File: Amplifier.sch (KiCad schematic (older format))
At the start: 52 parts, among them J501 TB001-500-04BE CUI_Devices, SW501 DS04-254-2-02BK-SMT, U501 TDA7498L

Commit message: fertig zum routen
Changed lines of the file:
@@
 $EndComp
 Wire Wire Line
-	6500 3500 8250 3500
+	6500 3500 7300 3500
 Connection ~ 8250 3500
 Wire Wire Line
@@
 	1    0    0    -1
 $EndComp
+$Comp
+L power:PWR_FLAG #FLG0114
+U 1 1 5E990599
+P 7300 3500
+F 0 "#FLG0114" H 7300 3575 50  0001 C CNN
+F 1 "PWR_FLAG" H 7550 3600 50  0000 C CNN
+F 2 "" H 7300 3500 50  0001 C CNN
+F 3 "~" H 7300 3500 50  0001 C CNN
+	1    7300 3500
+	1    0    0    -1
+$EndComp
+Connection ~ 7300 3500
+Wire Wire Line
+	7300 3500 8250 3500
 $EndSCHEMATC

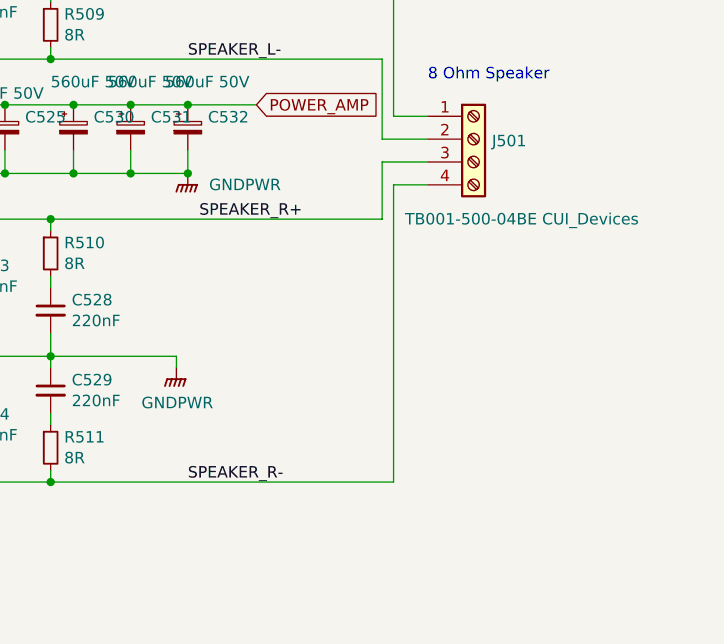
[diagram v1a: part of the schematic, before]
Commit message: Amp verdrahtet, Einige Layers verlegt
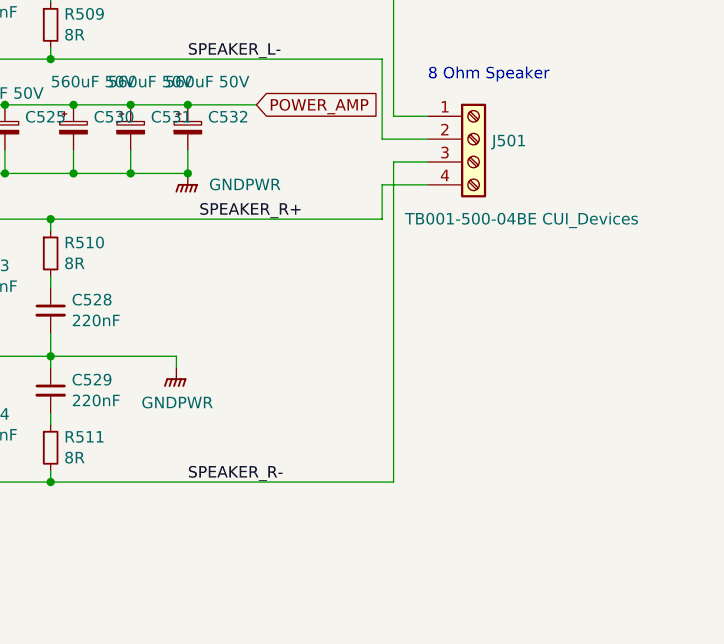
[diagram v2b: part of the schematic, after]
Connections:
- net SPEAKER_R+: now also J501.4 (Pin_4); no longer J501.3 (Pin_3)
- net SPEAKER_R-: now also J501.3 (Pin_3); no longer J501.4 (Pin_4)
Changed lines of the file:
@@
 	8450 2150 9950 2150
 Wire Wire Line
-	10100 3850 9950 3850
-Wire Wire Line
-	9950 3850 9950 5150
-Wire Wire Line
 	8450 5150 9950 5150
 Wire Wire Line
-	10100 3750 9900 3750
-Wire Wire Line
-	9900 3750 9900 4000
+	9900 3850 9900 4000
 Wire Wire Line
 	8450 4000 9900 4000
@@
 Wire Wire Line
 	7300 3500 8250 3500
+Wire Wire Line
+	9950 3750 10100 3750
+Wire Wire Line
+	9950 3750 9950 5150
+Wire Wire Line
+	9900 3850 10100 3850
 $EndSCHEMATC

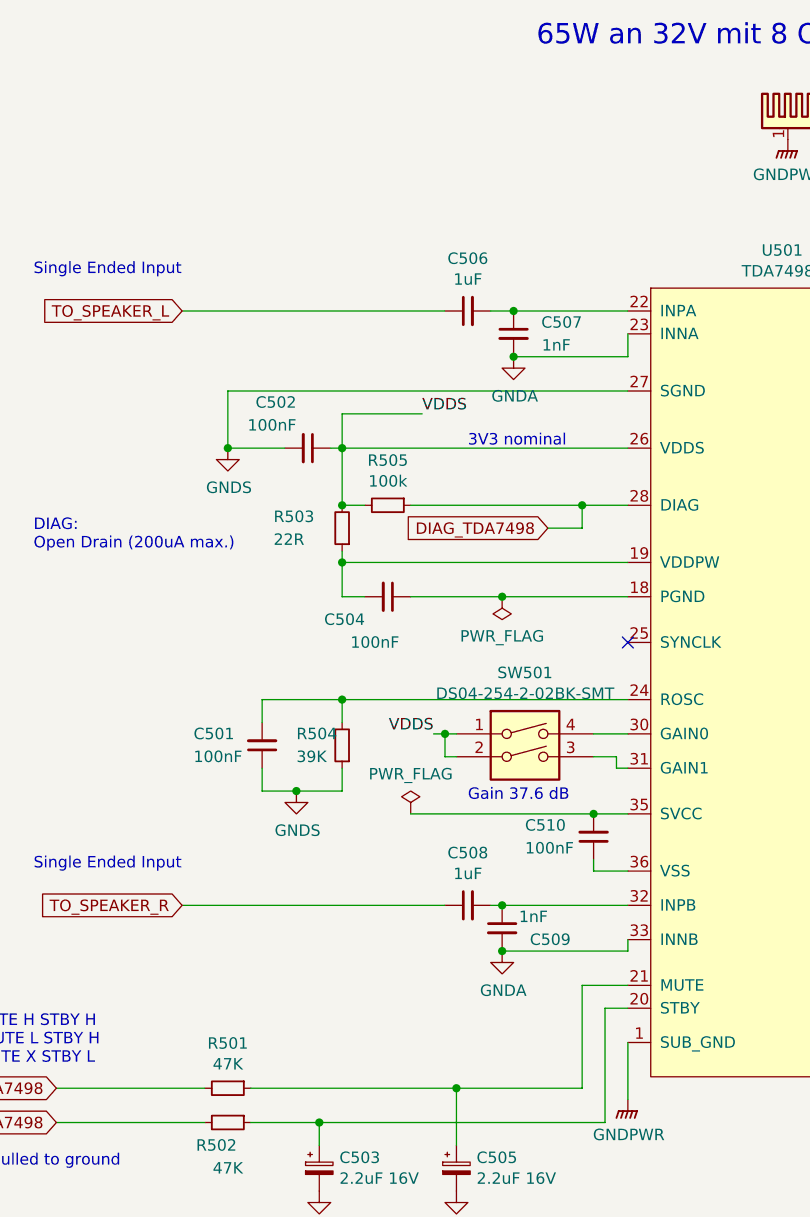
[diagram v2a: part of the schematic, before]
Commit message: Folienkondensatoren SMD gegen THT ausgetauscht. Kleine Fehler korrigiert
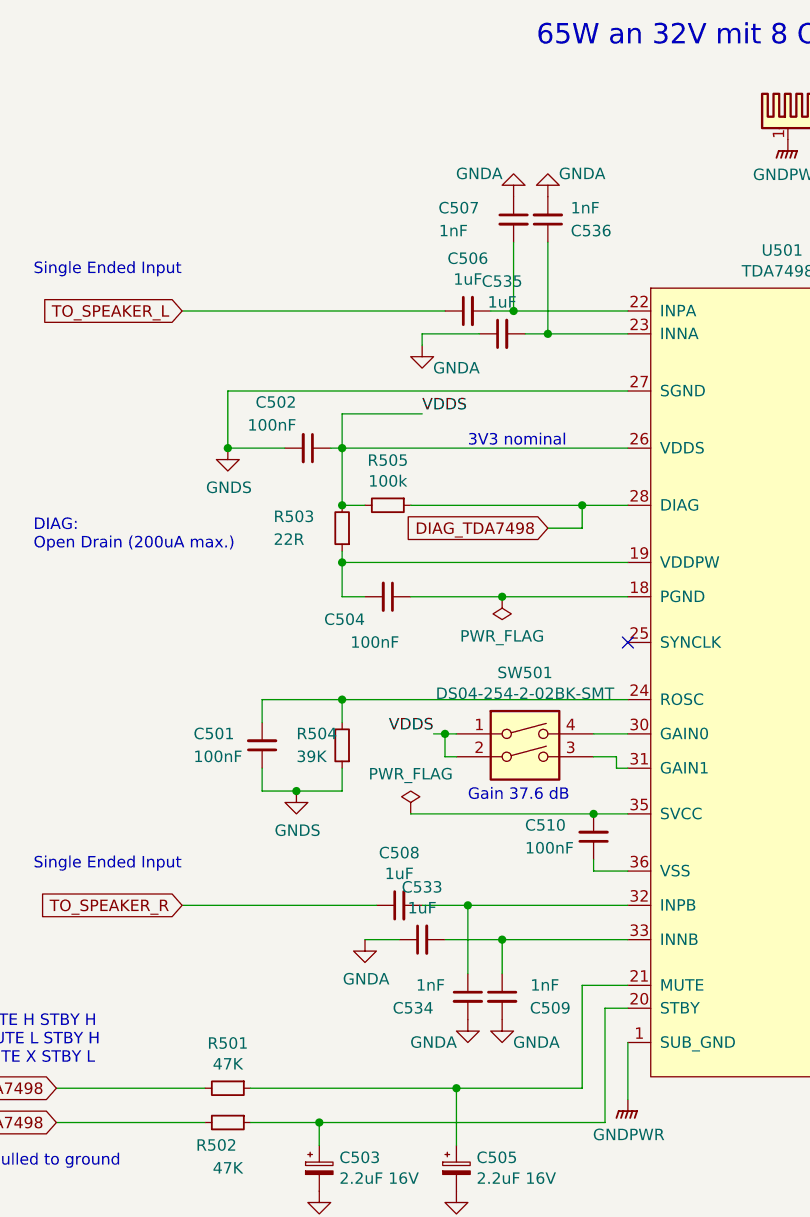
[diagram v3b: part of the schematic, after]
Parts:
- added C533, C535: 1uF, Capacitor_THT:C_Rect_L7.0mm_W2.5mm_P5.00mm, symbol Device:C_Small
- added C534, C536: 1nF, Capacitor_THT:C_Rect_L7.0mm_W2.5mm_P5.00mm, symbol Device:C_Small
- C506, C507, C508, C509, C517, C518, C519, C520, C521, C522, C523, C524, C526, C527, C528, C529: footprint Capacitor_SMD:C_0603_1608Metric_Pad1.05x0.95mm_HandSolder -> Capacitor_THT:C_Rect_L7.0mm_W2.5mm_P5.00mm
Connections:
- net GNDA: now also C507.1, C533.1, C534.2, C535.1, C536.2; no longer C507.2, U501.23 (INNA), U501.33 (INNB)
- net at C506.2, U501.22 (INPA): now also C507.2; no longer C507.1
- net at C508.2, U501.32 (INPB): now also C534.1; no longer C509.1
- new net: C535.2, C536.1, U501.23 (INNA)
- new net: C509.1, C533.2, U501.33 (INNB)
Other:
- moved on the sheet: C507, C508, C509

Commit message: layout fast fertig
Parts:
- removed C506, C508: 1uF, Capacitor_THT:C_Rect_L7.0mm_W2.5mm_P5.00mm, symbol Device:C_Small
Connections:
- net TO_SPEAKER_L: now also C507.2, U501.22 (INPA)
- net TO_SPEAKER_R: now also C534.1, U501.32 (INPB)
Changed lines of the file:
@@
 TO_SPEAKER_R
-$Comp
-L Device:C_Small C506
-U 1 1 5E7A16FA
-P 4050 2150
-F 0 "C506" V 4279 2150 50  0000 C CNN
-F 1 "1uF" V 4188 2150 50  0000 C CNN
-F 2 "Capacitor_THT:C_Rect_L7.0mm_W2.5mm_P5.00mm" H 4050 2150 50  0001 C CNN
-F 3 "~" H 4050 2150 50  0001 C CNN
-	1    4050 2150
-	0    -1   -1   0
-$EndComp
 $Comp
 L Device:C_Small C507
@@
 	4600 4600 4600 4550
 $Comp
-L Device:C_Small C508
-U 1 1 5E8A8398
-P 3750 4750
-F 0 "C508" V 3979 4750 50  0000 C CNN
-F 1 "1uF" V 3888 4750 50  0000 C CNN
-F 2 "Capacitor_THT:C_Rect_L7.0mm_W2.5mm_P5.00mm" H 3750 4750 50  0001 C CNN
-F 3 "~" H 3750 4750 50  0001 C CNN
-	1    3750 4750
-	0    -1   -1   0
-$EndComp
-$Comp
 L Device:C_Small C509
 U 1 1 5E8B9322
@@
 	1    0    0    -1
 $EndComp
-Wire Wire Line
-	3650 4750 2800 4750
 $Comp
 L Device:CP_Small C505
@@
 Wire Wire Line
 	3000 2500 4750 2500
-Wire Wire Line
-	2800 2150 3950 2150
 Text Notes 2150 4600 0    50   ~ 0
 Single Ended Input
@@
 	-1   0    0    1
 $EndComp
-Wire Wire Line
-	4150 2150 4250 2150
 $Comp
 L power:GNDA #PWR0508
@@
 	1    0    0    -1
 $EndComp
-Wire Wire Line
-	3850 4750 4050 4750
 $Comp
 L Device:C_Small C533
@@
 Wire Wire Line
 	3750 4900 3600 4900
+Wire Wire Line
+	2800 4750 4050 4750
+Wire Wire Line
+	2800 2150 4250 2150
 $EndSCHEMATC

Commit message: Fertig zum letzten Check vor Bestellung
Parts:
- C503, C505: footprint Capacitor_SMD:CP_Elec_4x5.4 -> Capacitor_THT:CP_Radial_D4.0mm_P2.00mm
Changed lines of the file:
@@
 F 0 "C505" H 4088 5946 50  0000 L CNN
 F 1 "2.2uF 16V" H 4088 5855 50  0000 L CNN
-F 2 "Capacitor_SMD:CP_Elec_4x5.4" H 4000 5900 50  0001 C CNN
+F 2 "Capacitor_THT:CP_Radial_D4.0mm_P2.00mm" H 4000 5900 50  0001 C CNN
 F 3 "~" H 4000 5900 50  0001 C CNN
 	1    4000 5900
@@
 F 0 "C503" H 3488 5946 50  0000 L CNN
 F 1 "2.2uF 16V" H 3488 5855 50  0000 L CNN
-F 2 "Capacitor_SMD:CP_Elec_4x5.4" H 3400 5900 50  0001 C CNN
+F 2 "Capacitor_THT:CP_Radial_D4.0mm_P2.00mm" H 3400 5900 50  0001 C CNN
 F 3 "~" H 3400 5900 50  0001 C CNN
 	1    3400 5900

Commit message: Board abgeschickt
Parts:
- C517, C518: value 330pF -> 1nF
- C533, C535: value 1uF -> 100nF
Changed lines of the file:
@@
 P 6900 3050
 F 0 "C517" H 7000 3250 50  0000 L CNN
-F 1 "330pF" H 7000 3150 50  0000 L CNN
+F 1 "1nF" H 7000 3150 50  0000 L CNN
 F 2 "Capacitor_THT:C_Rect_L7.0mm_W2.5mm_P5.00mm" H 6900 3050 50  0001 C CNN
 F 3 "~" H 6900 3050 50  0001 C CNN
@@
 P 6900 4900
 F 0 "C518" H 6992 4946 50  0000 L CNN
-F 1 "330pF" H 6992 4855 50  0000 L CNN
+F 1 "1nF" H 6992 4855 50  0000 L CNN
 F 2 "Capacitor_THT:C_Rect_L7.0mm_W2.5mm_P5.00mm" H 6900 4900 50  0001 C CNN
 F 3 "~" H 6900 4900 50  0001 C CNN
@@
 P 4200 2250
 F 0 "C535" V 4429 2250 50  0000 C CNN
-F 1 "1uF" V 4338 2250 50  0000 C CNN
+F 1 "100nF" V 4338 2250 50  0000 C CNN
 F 2 "Capacitor_THT:C_Rect_L7.0mm_W2.5mm_P5.00mm" H 4200 2250 50  0001 C CNN
 F 3 "~" H 4200 2250 50  0001 C CNN
@@
 P 3850 4900
 F 0 "C533" V 4079 4900 50  0000 C CNN
-F 1 "1uF" V 3988 4900 50  0000 C CNN
+F 1 "100nF" V 3988 4900 50  0000 C CNN
 F 2 "Capacitor_THT:C_Rect_L7.0mm_W2.5mm_P5.00mm" H 3850 4900 50  0001 C CNN
 F 3 "~" H 3850 4900 50  0001 C CNN

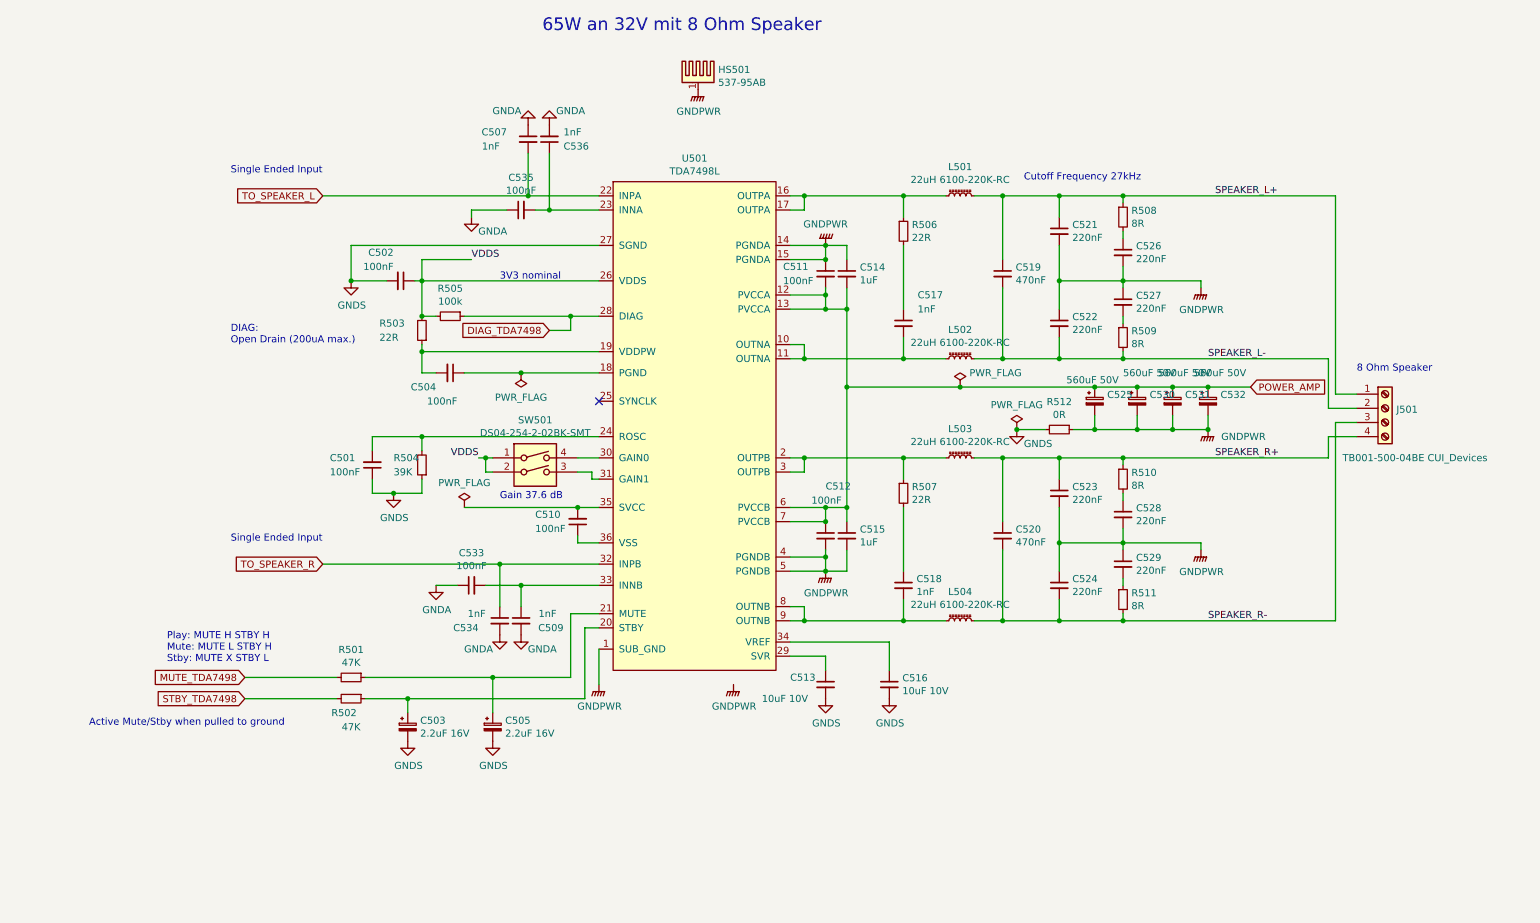
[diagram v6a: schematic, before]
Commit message: mute and stdby tda7498 geändert, tda7418 durch tda7719 ersetzt, xs3868 durch bk8000l ersetzt, 3v3 stepdown statt LDO. BMS gelöscht.  TODO: Möglichkeit stepup und stepdown als modul aufzusetzen
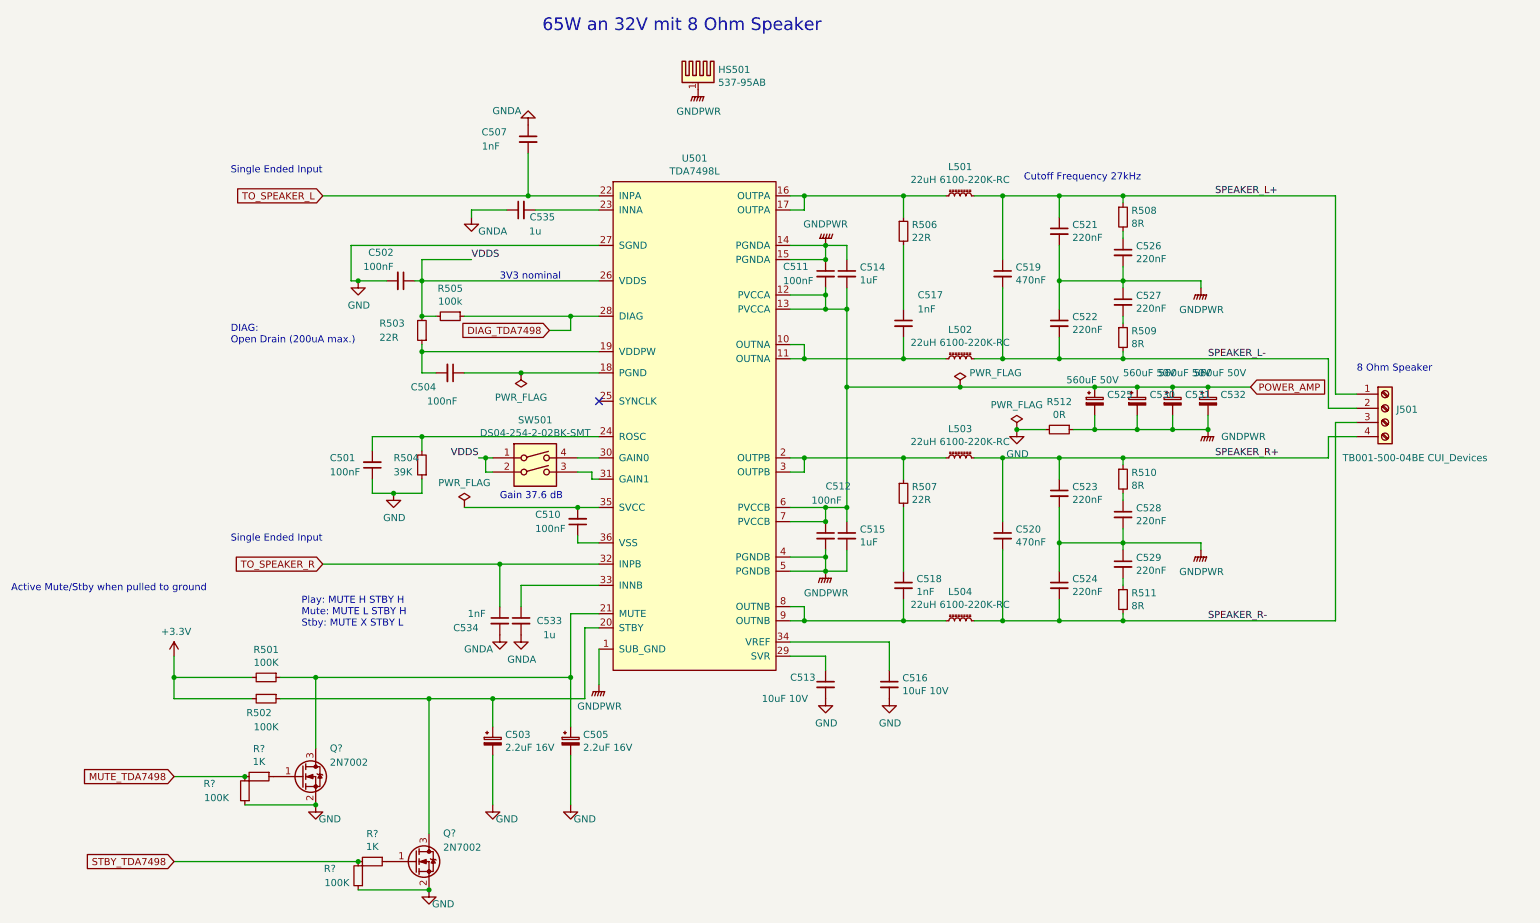
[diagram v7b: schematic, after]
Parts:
- removed C509, C536: 1nF, Capacitor_THT:C_Rect_L7.0mm_W2.5mm_P5.00mm, symbol Device:C_Small
- added Q? (x2): 2N7002, Package_TO_SOT_SMD:SOT-23, symbol Transistor_FET:2N7002
- added R? (x2): 100K, Resistor_SMD:R_0603_1608Metric_Pad1.05x0.95mm_HandSolder, symbol Device:R_Small
- added R? (x2): 1K, Resistor_SMD:R_0603_1608Metric_Pad1.05x0.95mm_HandSolder, symbol Device:R_Small
- C533, C535: value 100nF -> 1u; footprint Capacitor_THT:C_Rect_L7.0mm_W2.5mm_P5.00mm -> Capacitor_THT:C_Rect_L7.2mm_W7.2mm_P5.00mm_FKS2_FKP2_MKS2_MKP2
- R501, R502: value 47K -> 100K
- R512: footprint Resistor_SMD:R_0603_1608Metric_Pad1.05x0.95mm_HandSolder -> Resistor_SMD:R_1206_3216Metric_Pad1.42x1.75mm_HandSolder
- U501: footprint Package_SO:ST_PowerSSO-36_SlugDown_ThermalVias -> Package_SO:ST_PowerSSO-36_TDA7498
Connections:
- net GNDA: now also C533.2; no longer C533.1
- net MUTE_TDA7498: now also R?.2, R?.2; no longer R501.2
- net STBY_TDA7498: now also R?.2, R?.2; no longer R502.2
- net at C503.1, R502.1, U501.20 (STBY): now also Q?.3 (D)
- net at C505.1, R501.1, U501.21 (MUTE): now also Q?.3 (D)
- net at U501.33 (INNB): now also C533.1; no longer C533.2
- net GNDS renamed GND
- net GND: now also Q?.2 (S), Q?.2 (S), R?.1, R?.1
- new net: Q?.1 (G), R?.1 (x2)
- new net +3V3: R501.2, R502.2
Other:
- moved on the sheet: C503, C505, C533, R501, R502
